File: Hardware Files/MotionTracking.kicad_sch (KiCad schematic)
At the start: 6 parts, among them IC1 STM32F411RET6, J1 Micro_SD_Card_Det1, U1 LSM6DSV16XTR, U2 LSM6DSV16XTR, U3 LSM6DSV16XTR

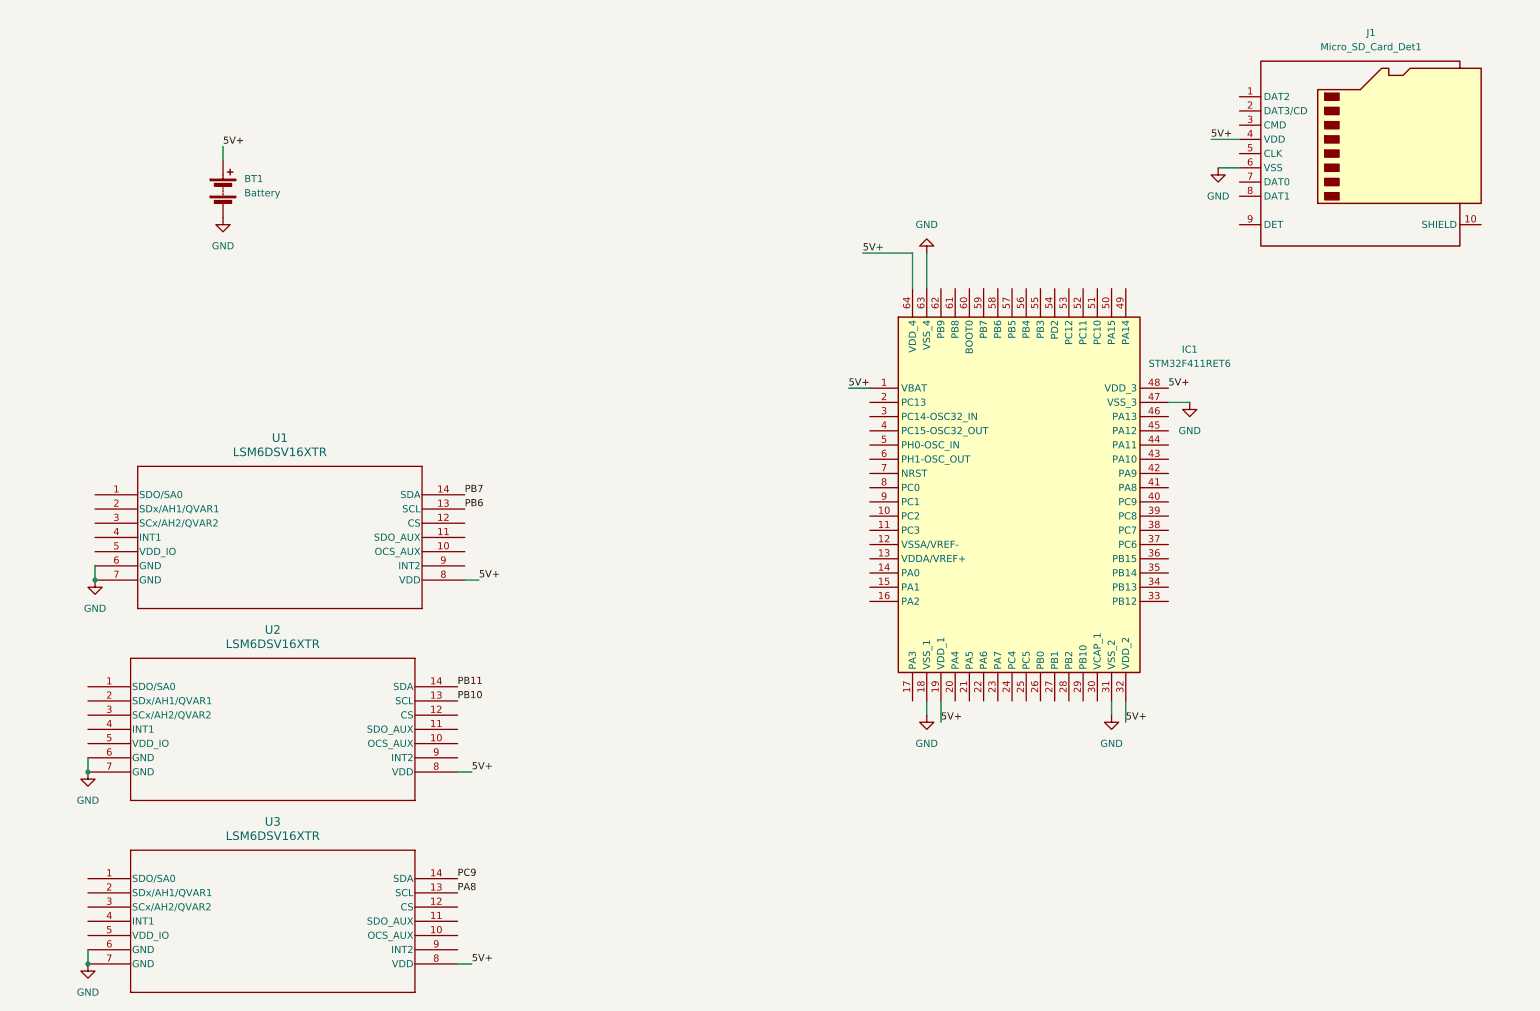
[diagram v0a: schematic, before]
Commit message: Decoupling Caps, Pull Ups, Diodes
- Added decoupling caps according to design notes

- Pulled I2C lines to VSS as specified by IMU datasheet

-Added Shottky diodes to main power to select between 5V USB and 5V from battery.
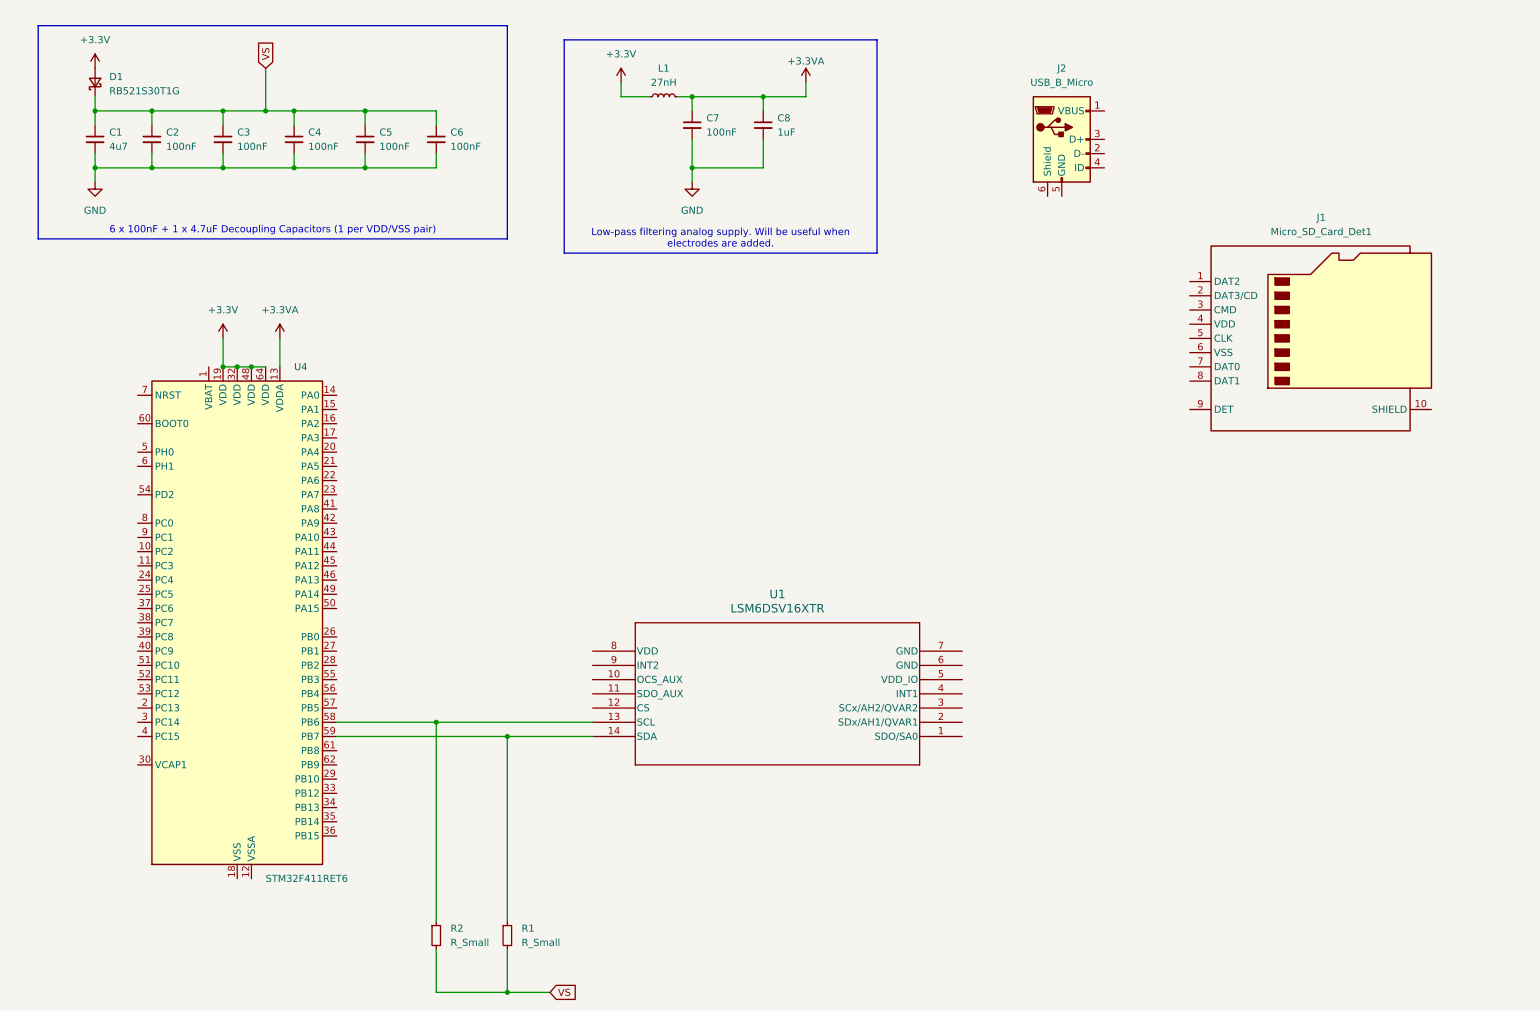
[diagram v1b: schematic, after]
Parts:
- removed BT1: Battery, symbol Device:Battery
- removed IC1: STM32F411RET6, QFP50P1200X1200X160-64N, symbol mcu:STM32F411RET6
- removed U2, U3: LSM6DSV16XTR, LGA14L_LSM6_STM, symbol imu:LSM6DSV16XTR
- added C1: 4u7, symbol Device:C_Small
- added C2, C3, C4, C5, C6, C7: 100nF, symbol Device:C_Small
- added C8: 1uF, symbol Device:C_Small
- added D1: RB521S30T1G, symbol Device:D_Schottky_Small
- added J2: USB_B_Micro, symbol Connector:USB_B_Micro
- added L1: 27nH, symbol Device:L_Small
- added R1, R2: R_Small, symbol Device:R_Small
- added U4: STM32F411RET6, Package_QFP:LQFP-64_10x10mm_P0.5mm, symbol MCU_ST_STM32F4:STM32F411RETx
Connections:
- net GND: now also C1.2, C2.2, C3.2, C4.2, C5.2, C6.2, C7.2, C8.2; no longer J1.6 (VSS), U1.6 (GND), U1.7 (GND)
- net 5V+: no longer names the net of J1.4 (VDD)
- net 5V+: no longer U1.8 (VDD)
- net PB6: no longer names the net of U1.13 (SCL)
- net PB6: now also R2.1, U4.58 (PB6)
- net PB7: no longer names the net of U1.14 (SDA)
- net PB7: now also R1.1, U4.59 (PB7)
- new net: U4.18 (VSS), U4.31 (VSS), U4.47 (VSS), U4.63 (VSS)
- new net +3.3V: D1.2 (A), L1.1, U4.19 (VDD), U4.32 (VDD), U4.48 (VDD), U4.64 (VDD)
- new net +3.3VA: C7.1, C8.1, L1.2, U4.13 (VDDA)
- new net VS: C1.1, C2.1, C3.1, C4.1, C5.1, C6.1, D1.1 (K), R1.2, R2.2
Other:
- company: (none) -> Alberta Bionix
- title: (none) -> STM32F411 Motion Tracker
- moved on the sheet: J1, U1

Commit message: Added circuitry for oscillator
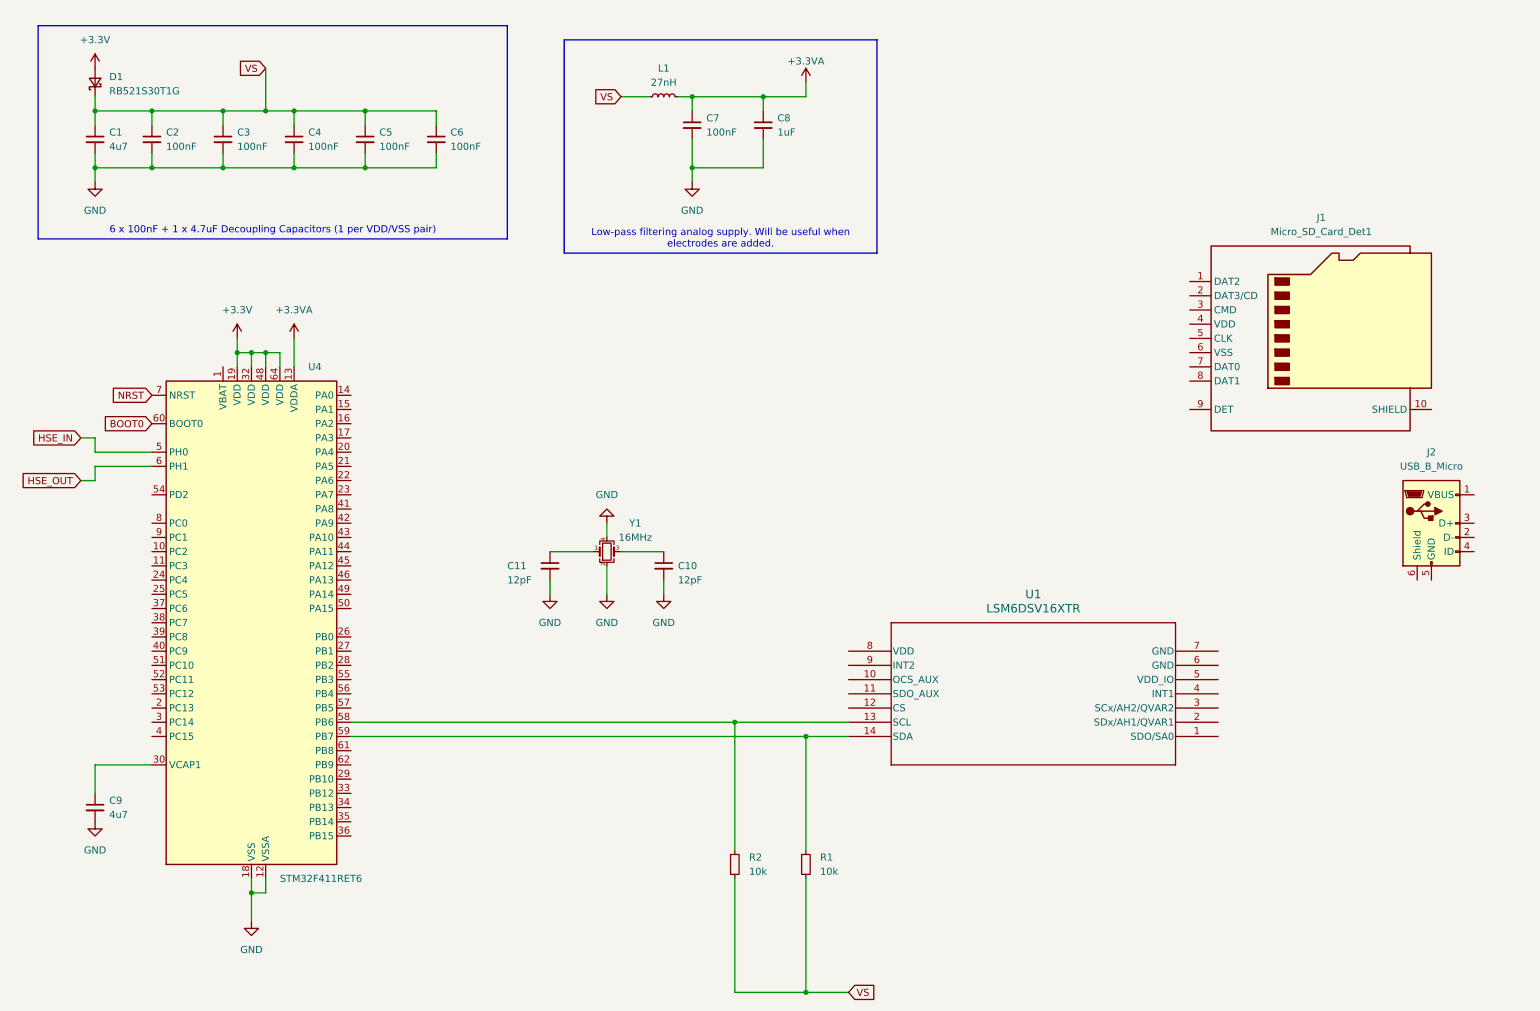
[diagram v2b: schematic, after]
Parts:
- added C10, C11: 12pF, symbol Device:C_Small
- added C9: 4u7, symbol Device:C_Small
- added Y1: 16MHz, symbol Device:Crystal_GND24_Small
- R1, R2: value R_Small -> 10k
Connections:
- net +3.3V: no longer L1.1
- net GND: now also U4.12 (VSSA), U4.18 (VSS), U4.31 (VSS), U4.47 (VSS), U4.63 (VSS), C10.2, C11.2, C9.2, Y1.2, Y1.4
- net VS: now also L1.1
- net at U4.30 (VCAP1): now also C9.1
- net HSE_IN: now reaches U4.5 (PH0)
- net HSE_OUT: now reaches U4.6 (PH1)
- net BOOT0: now reaches U4.60 (BOOT0)
- net NRST: now reaches U4.7 (NRST)
- new net: C10.1, Y1.3
- new net: C11.1, Y1.1
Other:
- moved on the sheet: J2, R1, R2, U1, U4

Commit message: Wired Pierce Oscillator
Updated circuit for external oscillator. Added labels for SD card interface.
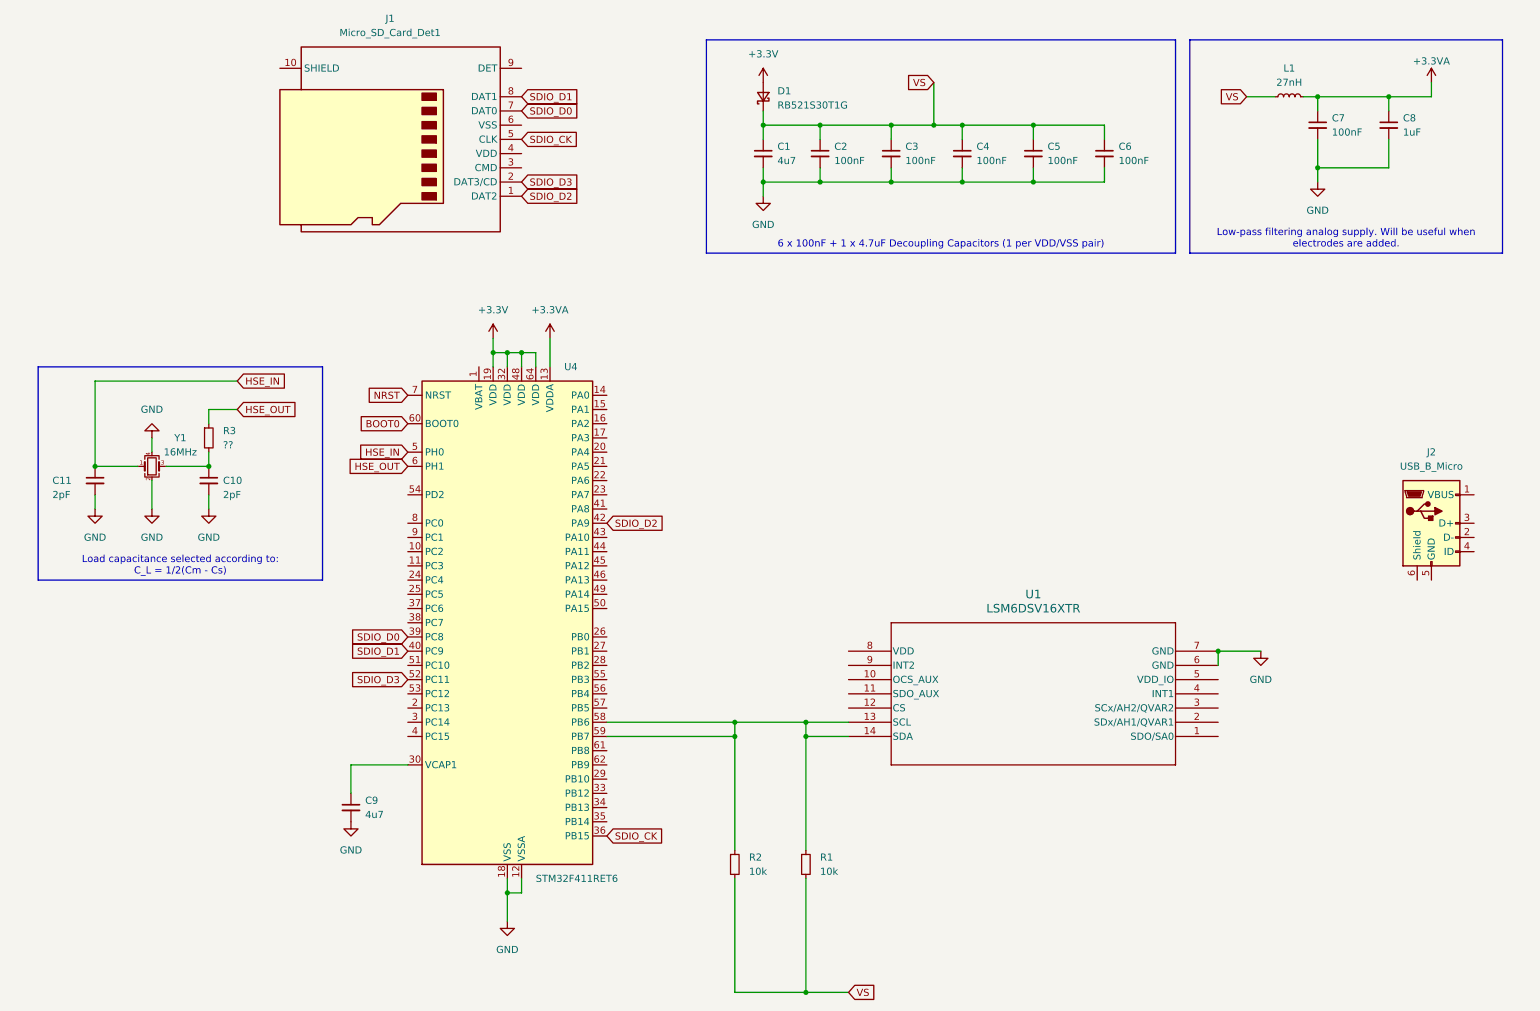
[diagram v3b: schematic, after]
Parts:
- added R3: ??, symbol Device:R_Small
- C10, C11: value 12pF -> 2pF
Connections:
- net GND: now also U1.6 (GND), U1.7 (GND)
- net HSE_IN: now also C11.1, Y1.1
- net HSE_OUT: now also R3.1
- net at C10.1, Y1.3: now also R3.2
- net at R2.1, U1.13 (SCL), U4.58 (PB6): now also R1.1, U1.14 (SDA), U4.59 (PB7)
- net SDIO_CK: now reaches U4.36 (PB15)
- net SDIO_CK: now also J1.5 (CLK)
- net SDIO_D0: now reaches U4.39 (PC8)
- net SDIO_D0: now also J1.7 (DAT0)
- net SDIO_D1: now reaches U4.40 (PC9)
- net SDIO_D1: now also J1.8 (DAT1)
- net SDIO_D2: now reaches U4.42 (PA9)
- net SDIO_D2: now also J1.1 (DAT2)
- net SDIO_D3: now reaches U4.52 (PC11)
- net SDIO_D3: now also J1.2 (DAT3/CD)
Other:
- moved on the sheet: C1, C10, C11, C2, C3, C4, C5, C6, C7, C8, C9, D1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

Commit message: Changed to SPI
Updated Schematic to use SPI interface. I2C3 controller pins overlapped with USB pins.
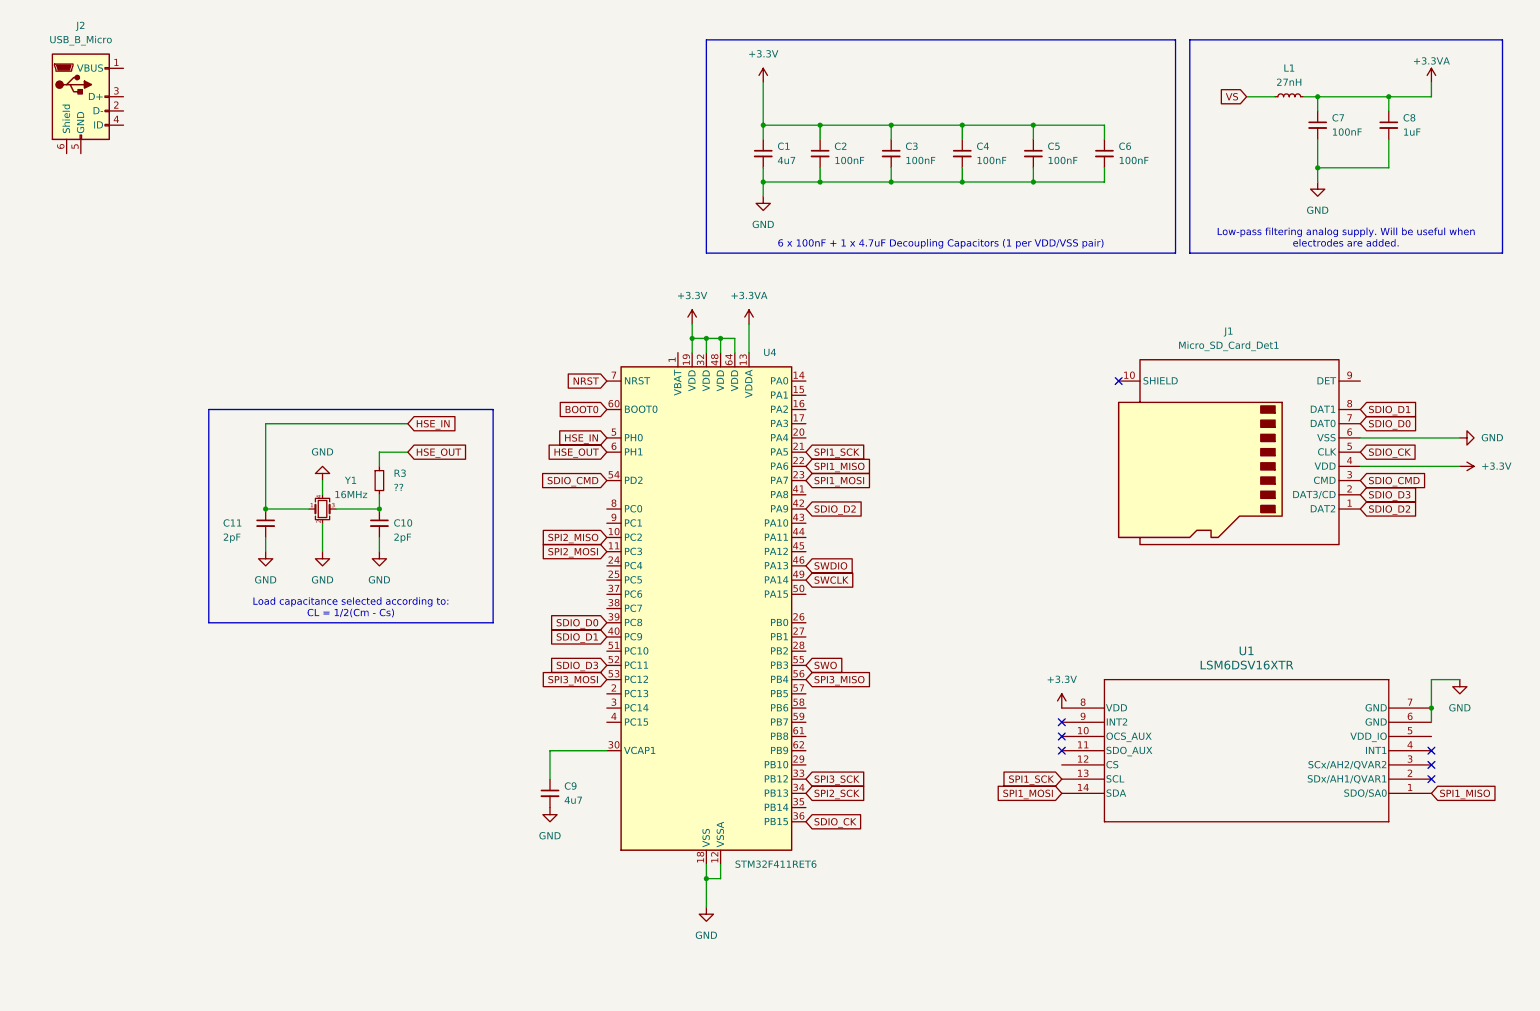
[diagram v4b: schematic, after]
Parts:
- removed D1: RB521S30T1G, symbol Device:D_Schottky_Small
- removed R1, R2: 10k, symbol Device:R_Small
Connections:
- net +3.3V: now also C1.1, C2.1, C3.1, C4.1, C5.1, C6.1, J1.4 (VDD), U1.8 (VDD)
- net GND: now also J1.6 (VSS)
- net VS: no longer C1.1, C2.1, C3.1, C4.1, C5.1, C6.1
- net SPI2_MISO: now reaches U4.10 (PC2)
- net SPI2_MOSI: now reaches U4.11 (PC3)
- net SPI1_SCK: now reaches U4.21 (PA5)
- net SPI1_SCK: now also U1.13 (SCL)
- net SPI1_MISO: now reaches U4.22 (PA6)
- net SPI1_MISO: now also U1.1 (SDO/SA0)
- net SPI1_MOSI: now reaches U4.23 (PA7)
- net SPI1_MOSI: now also U1.14 (SDA)
- net SPI3_SCK: now reaches U4.33 (PB12)
- net SPI2_SCK: now reaches U4.34 (PB13)
- net SWDIO: now reaches U4.46 (PA13)
- net SWCLK: now reaches U4.49 (PA14)
- net SPI3_MOSI: now reaches U4.53 (PC12)
- net SDIO_CMD: now reaches U4.54 (PD2)
- net SDIO_CMD: now also J1.3 (CMD)
- net SWO: now reaches U4.55 (PB3)
- net SPI3_MISO: now reaches U4.56 (PB4)
- now unconnected: U4.58 (PB6), U4.59 (PB7)
- no-connect marks 0 -> 7
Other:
- moved on the sheet: C10, C11, C9, J1, J2, R3, U1, U4, Y1
